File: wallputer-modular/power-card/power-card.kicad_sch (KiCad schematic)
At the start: 139 parts, among them J2 Power, Q1 FQP27P06, Q2 IRLZ44N, SW1 reset, U1 TLC555CD, U12 74HC04, U16 74HC04, U17 74HC04, U18 74HC04, U2 74HC04, U3 74HC04

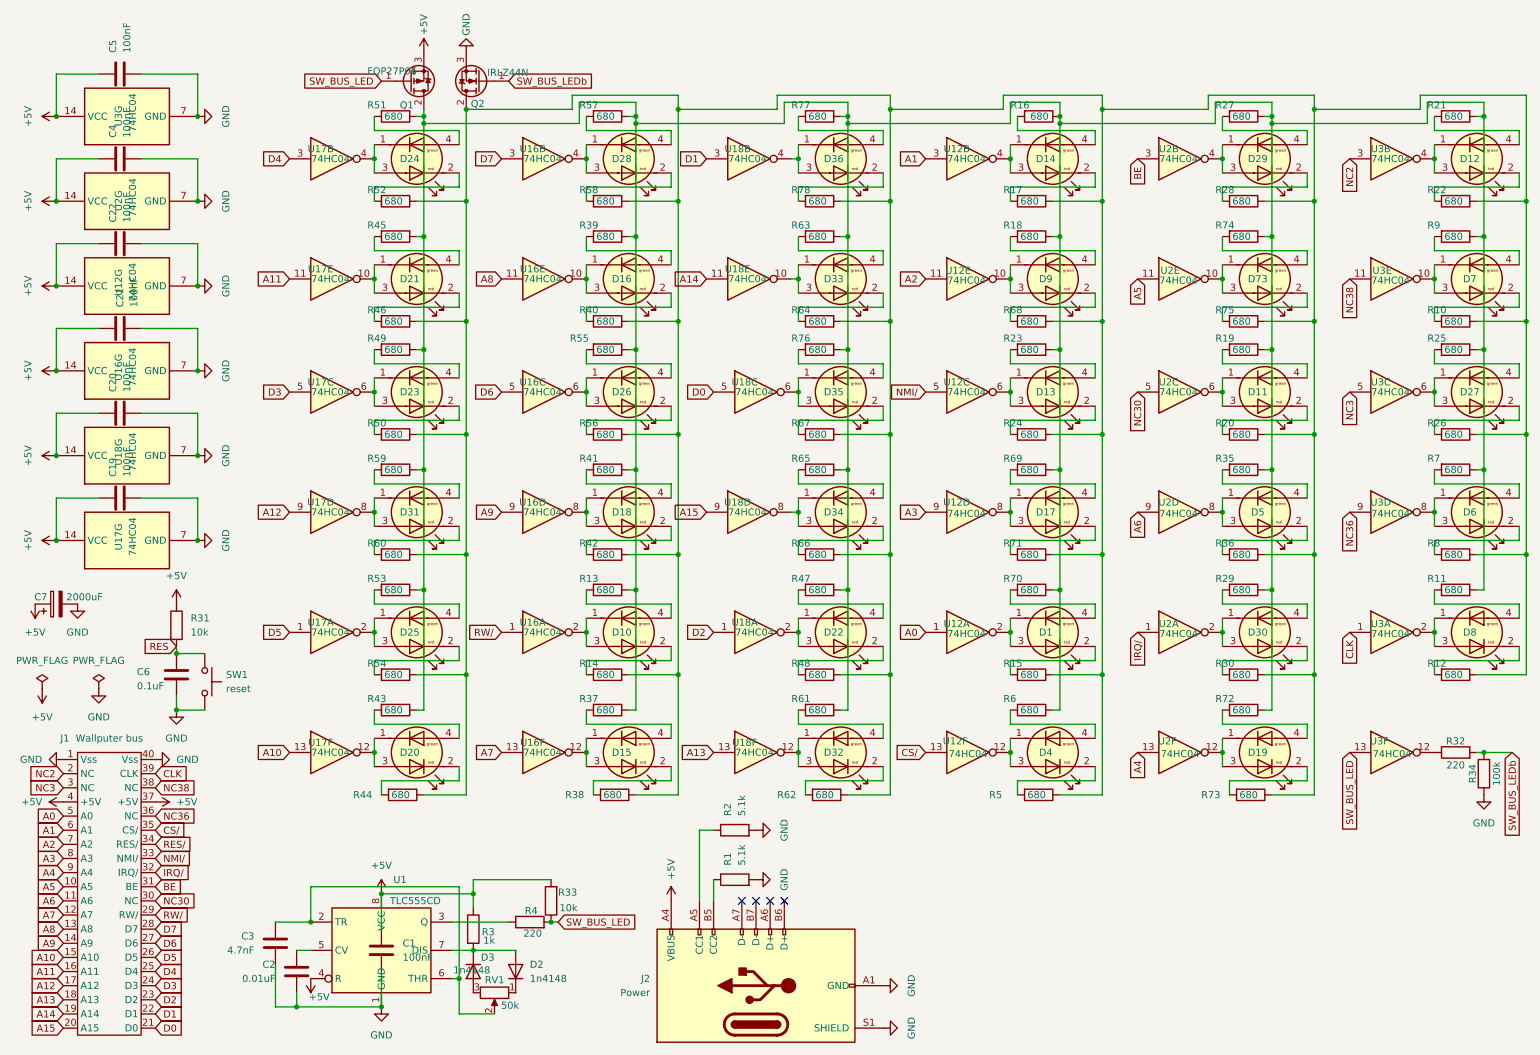
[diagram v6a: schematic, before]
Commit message: redesigning traces
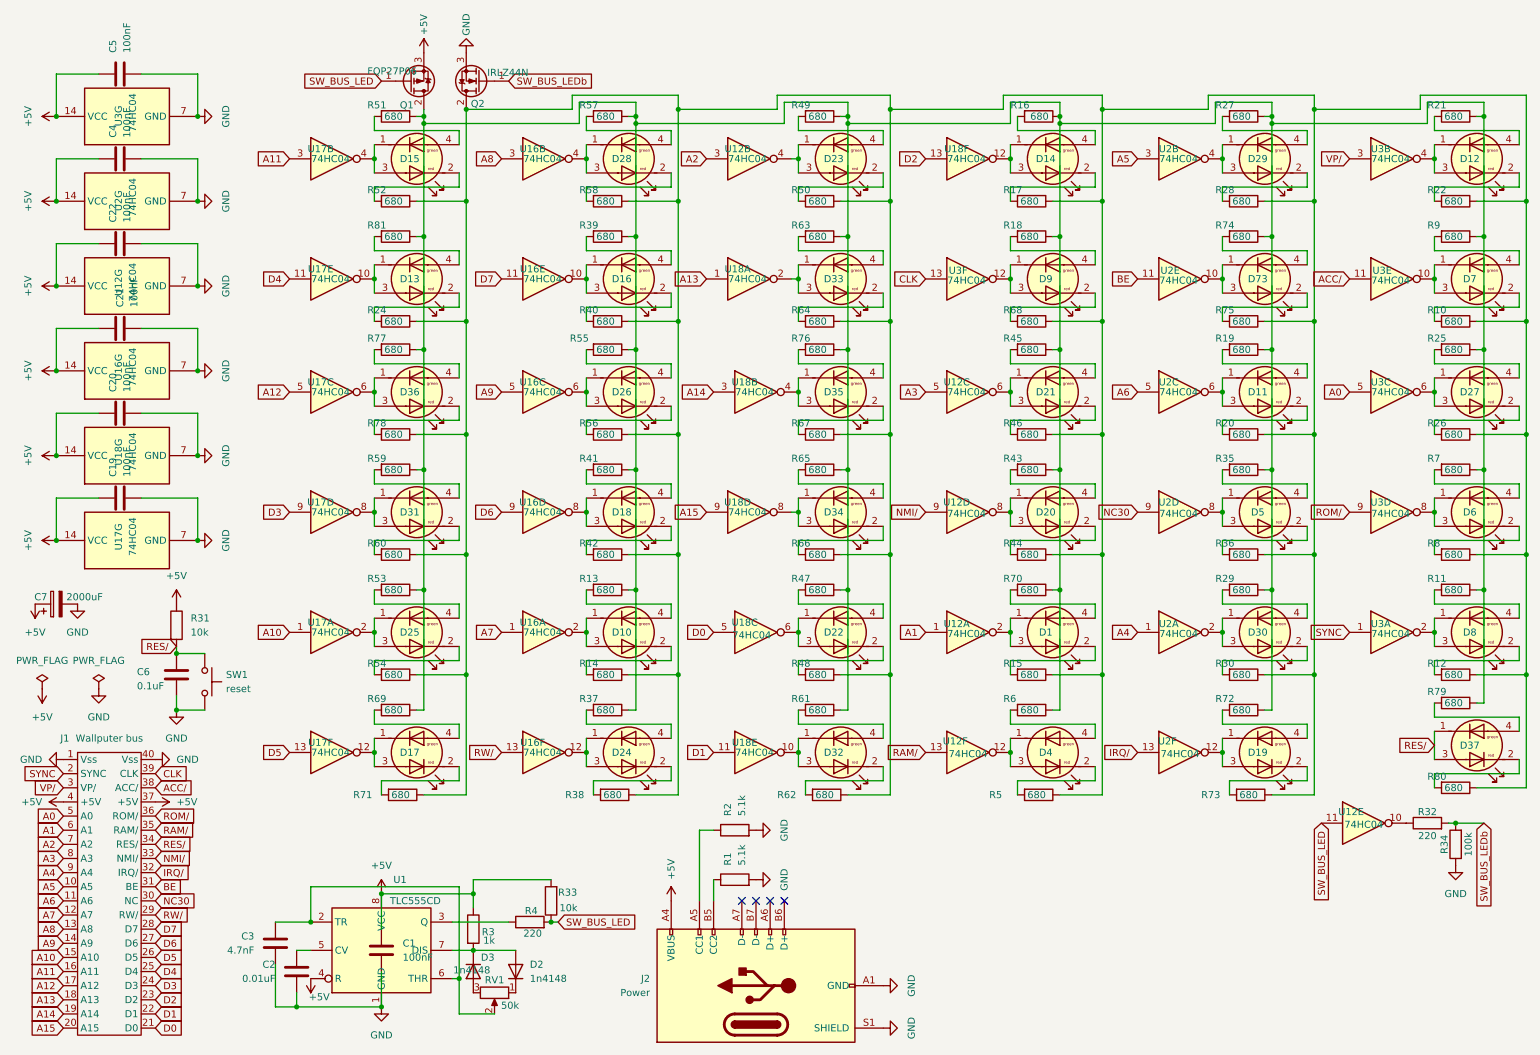
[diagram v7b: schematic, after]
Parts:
- removed R23: 680, Resistor_SMD:R_0603_1608Metric, symbol Device:R
- added D37: Wallputer_Dual_LED, Wallputer:Wallputer_Dual_LED, symbol Wallputer:Wallputer_Dual_LED
- added R79, R80, R81: 680, Resistor_SMD:R_0603_1608Metric, symbol Device:R
- renumbered D24 to D15, D20 to D17, D17 to D20, D15 to D24, R69 to R43, R71 to R44, R43 to R69, R44 to R71, U18 to U12, U3 to U12, U12 to U18, U12 to U3
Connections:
- net RES is gone; now on net RES/: C6.1, R31.2, SW1.1
- net A0: now also U3.5; no longer U12.1
- net A1: now also U12.1; no longer U18.3
- net A10: now also U17.1; no longer U17.13
- net A11: now also U17.3; no longer U17.11
- net A12: now also U17.5; no longer U17.9
- net A13: now also U18.1; no longer U18.13
- net A14: now also U18.3; no longer U18.11
- net A2: now also U12.3; no longer U3.11
- net A3: now also U12.5; no longer U12.9
- net A4: now also U2.1; no longer U2.13
- net A5: now also U2.3; no longer U2.11
- net A6: now also U2.5; no longer U2.9
- net A7: now also U16.1; no longer U16.13
- net A8: now also U16.3; no longer U16.11
- net A9: now also U16.5; no longer U16.9
- net BE: now also U2.11; no longer U2.3
- net CLK: now also U3.13; no longer U3.1
- net D0: now also U18.5; no longer U18.5
- net D1: now also U18.11; no longer U12.3
- net D2: now also U18.13; no longer U18.1
- net D3: now also U17.9; no longer U17.5
- net D4: now also U17.11; no longer U17.3
- net D5: now also U17.13; no longer U17.1
- net D6: now also U16.9; no longer U16.5
- net D7: now also U16.11; no longer U16.3
- net IRQ/: now also U2.13; no longer U2.1
- net NC30: now also U2.9; no longer U2.5
- net NMI/: now also U12.9; no longer U12.5
- net RES/: now also D37.1 (Green_A), D37.3 (Red_K)
- net RW/: now also U16.13; no longer U16.1
- net SW_BUS_LED: now also U12.11; no longer U12.13
- net at Q2.2 (D), R10.1, R12.1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: now also R80.1
- net at Q1.2 (D), R11.1, R13.1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: now also R79.1, R81.1
- net at D13.4 (Green_K): now also R81.2
- net at D36.1 (Green_A), D36.3 (Red_K): now also U17.6; no longer U12.4
- net at D35.1 (Green_A), D35.3 (Red_K): now also U18.4; no longer U18.6
- net at D21.1 (Green_A), D21.3 (Red_K): now also U12.6; no longer U17.10
- net at R32.1: now also U12.10; no longer U12.12
- net at D14.1 (Green_A), D14.3 (Red_K): now also U18.12; no longer U18.4
- net at D13.1 (Green_A), D13.3 (Red_K): now also U17.10; no longer U12.6
- net at D9.1 (Green_A), D9.3 (Red_K): now also U3.12; no longer U3.10
- net at D33.1 (Green_A), D33.3 (Red_K): now also U18.2; no longer U18.10
- net at D22.1 (Green_A), D22.3 (Red_K): now also U18.6; no longer U18.2
- net at D23.1 (Green_A), D23.3 (Red_K): now also U12.4; no longer U17.6
- net at D32.1 (Green_A), D32.3 (Red_K): now also U18.10; no longer U18.12
- net CS/ renamed RAM/
- net NC2 renamed SYNC
- net SYNC: now also U3.1; no longer U3.3
- net NC3 renamed VP/
- net VP/: now also U3.3; no longer U3.5
- net NC36 renamed ROM/
- net NC38 renamed ACC/
- new net: D37.4 (Green_K), R79.2
- new net: D37.2 (Red_A), R80.2
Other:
- moved on the sheet: D21, D23, D36, R32, R34, R45, R46, R49, R50, R78, U12E

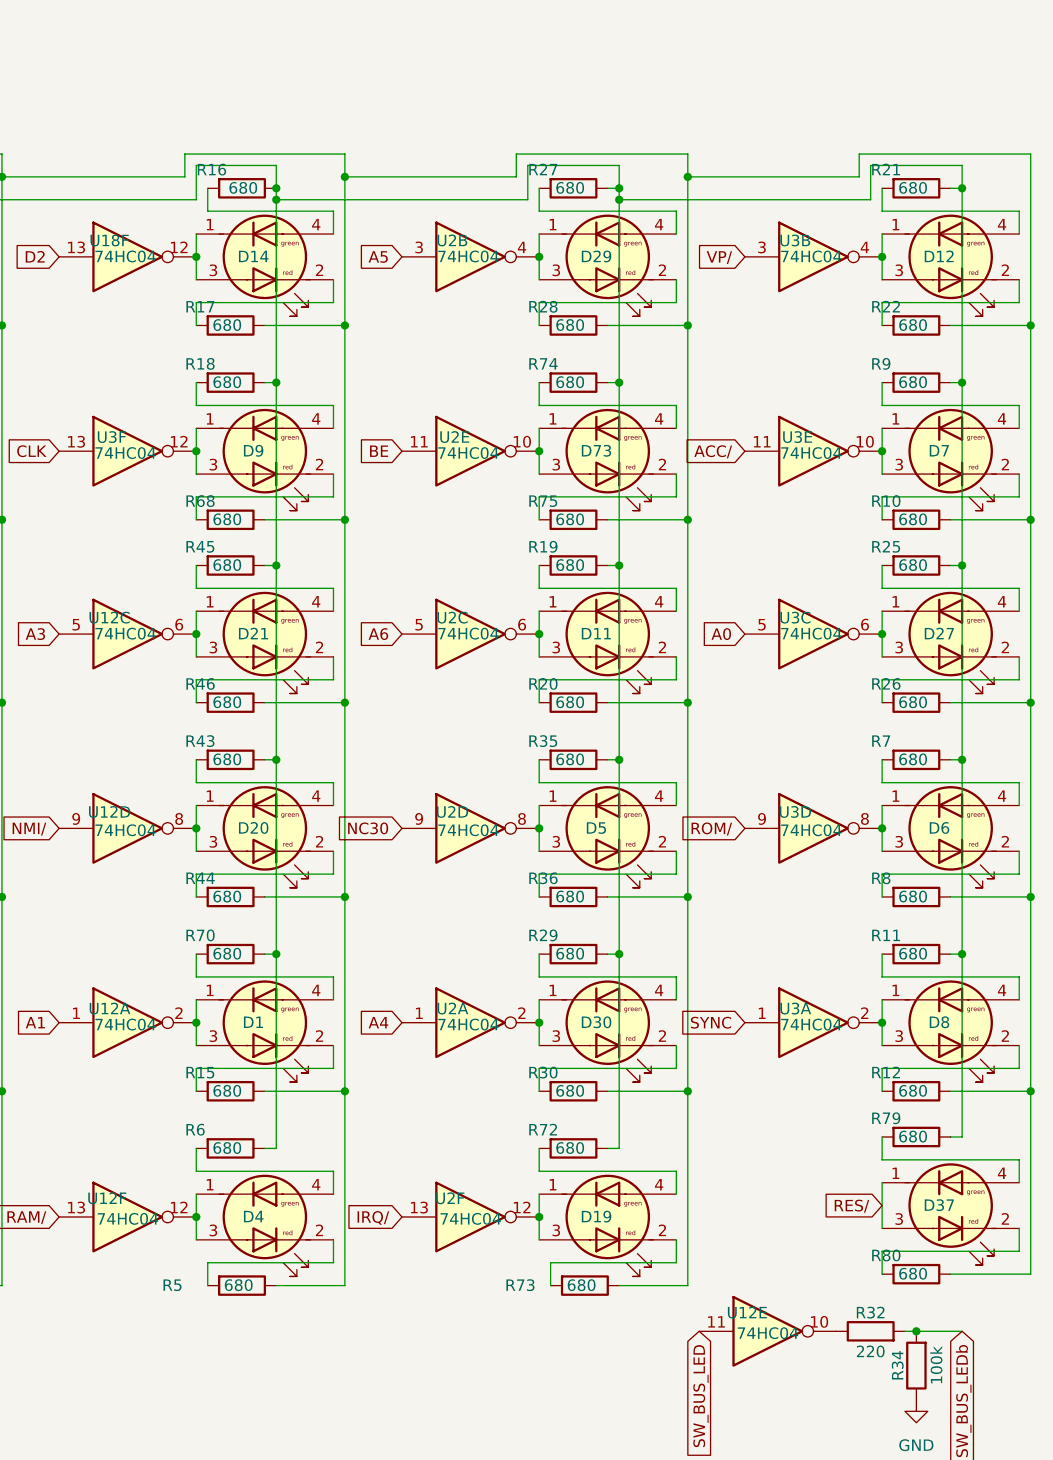
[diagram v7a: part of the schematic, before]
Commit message: replace dual leds with single for some signals
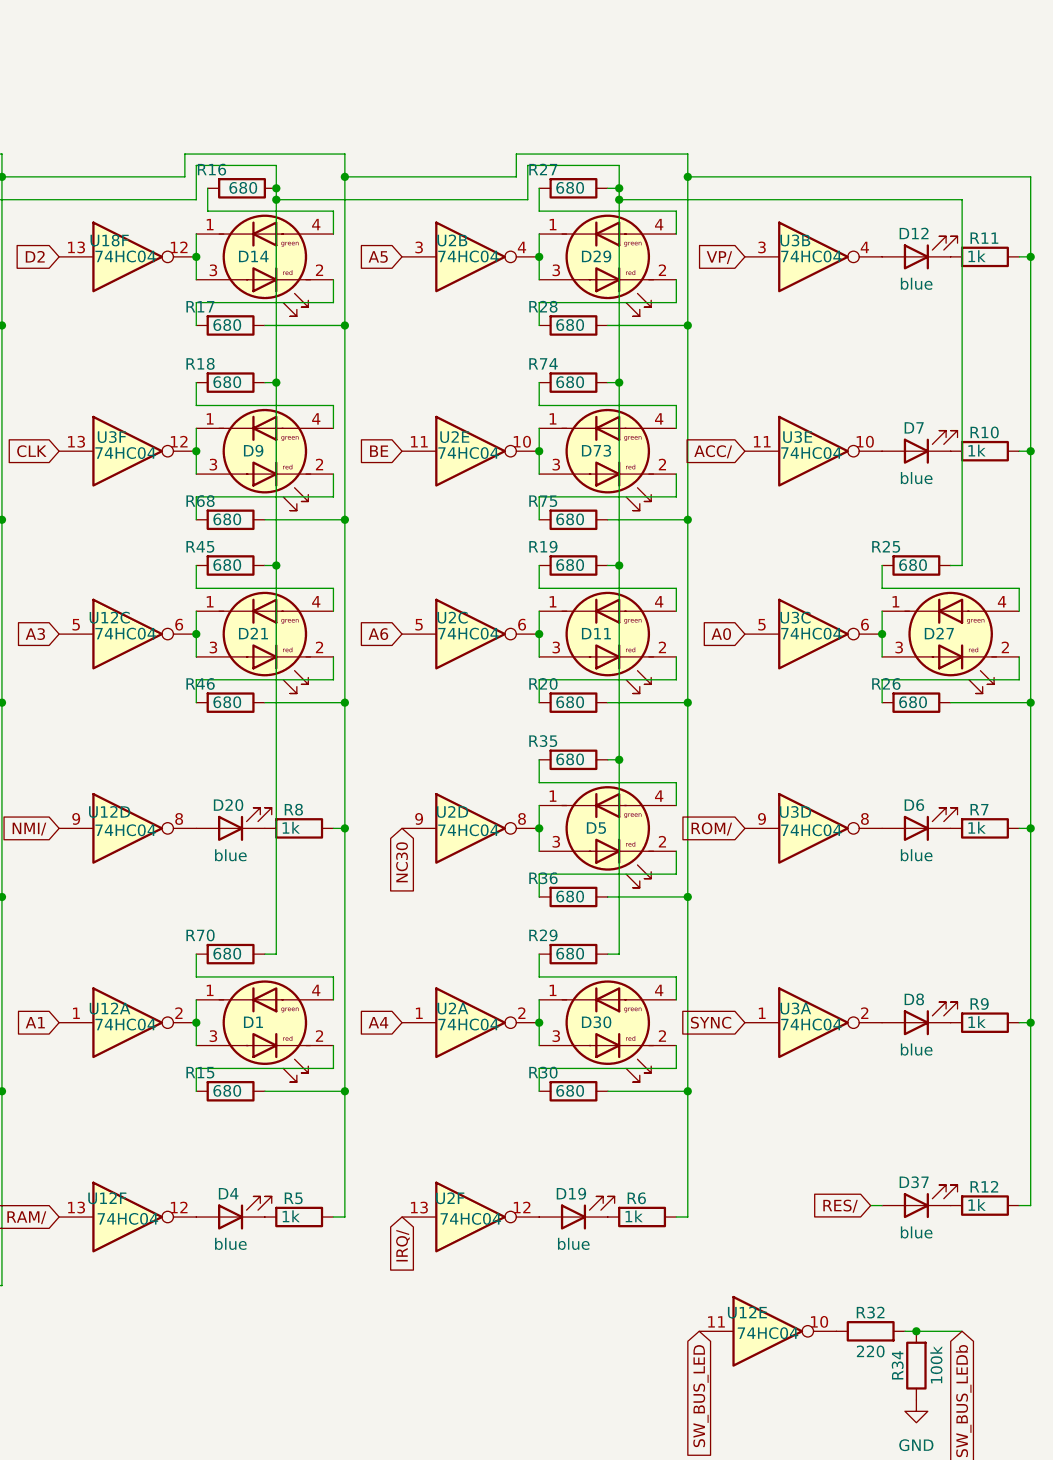
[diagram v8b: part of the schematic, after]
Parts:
- removed D12, D19, D20, D37, D4, D6, D7, D8: Wallputer_Dual_LED, Wallputer:Wallputer_Dual_LED, symbol Wallputer:Wallputer_Dual_LED
- removed R21, R22, R43, R44, R72, R73, R79, R80: 680, Resistor_SMD:R_0603_1608Metric, symbol Device:R
- added D12, D19, D20, D37, D4, D6, D7, D8: blue, LED_SMD:LED_1206_3216Metric, symbol Device:LED
- R10, R11, R12, R5, R6, R7, R8, R9: value 680 -> 1k
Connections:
- net RES/: now also D37.2 (A)
- net at Q2.2 (D), R10.1, R12.1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: now also R11.1, R6.1, R7.1, R9.1
- net at R5.2: now also D4.1 (K)
- net at Q1.2 (D), R13.1, R16.1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: no longer R11.1, R6.1, R7.1, R9.1
- net at U3.8: now also D6.2 (A)
- net at R8.2: now also D20.1 (K)
- net at R7.2: now also D6.1 (K)
- net at R6.2: now also D19.1 (K)
- net at U3.4: now also D12.2 (A)
- net at U12.8: now also D20.2 (A)
- net at R12.2: now also D37.1 (K)
- net at U3.10: now also D7.2 (A)
- net at R9.2: now also D8.1 (K)
- net at R10.2: now also D7.1 (K)
- net at U3.2: now also D8.2 (A)
- net at R11.2: now also D12.1 (K)
- net at U12.12: now also D4.2 (A)
- net at U2.12: now also D19.2 (A)
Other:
- moved on the sheet: R10
